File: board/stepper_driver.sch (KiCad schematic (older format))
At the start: 28 parts, among them J2301 CONN_STEPPER, P2301 CONN_2, U2301 L6470

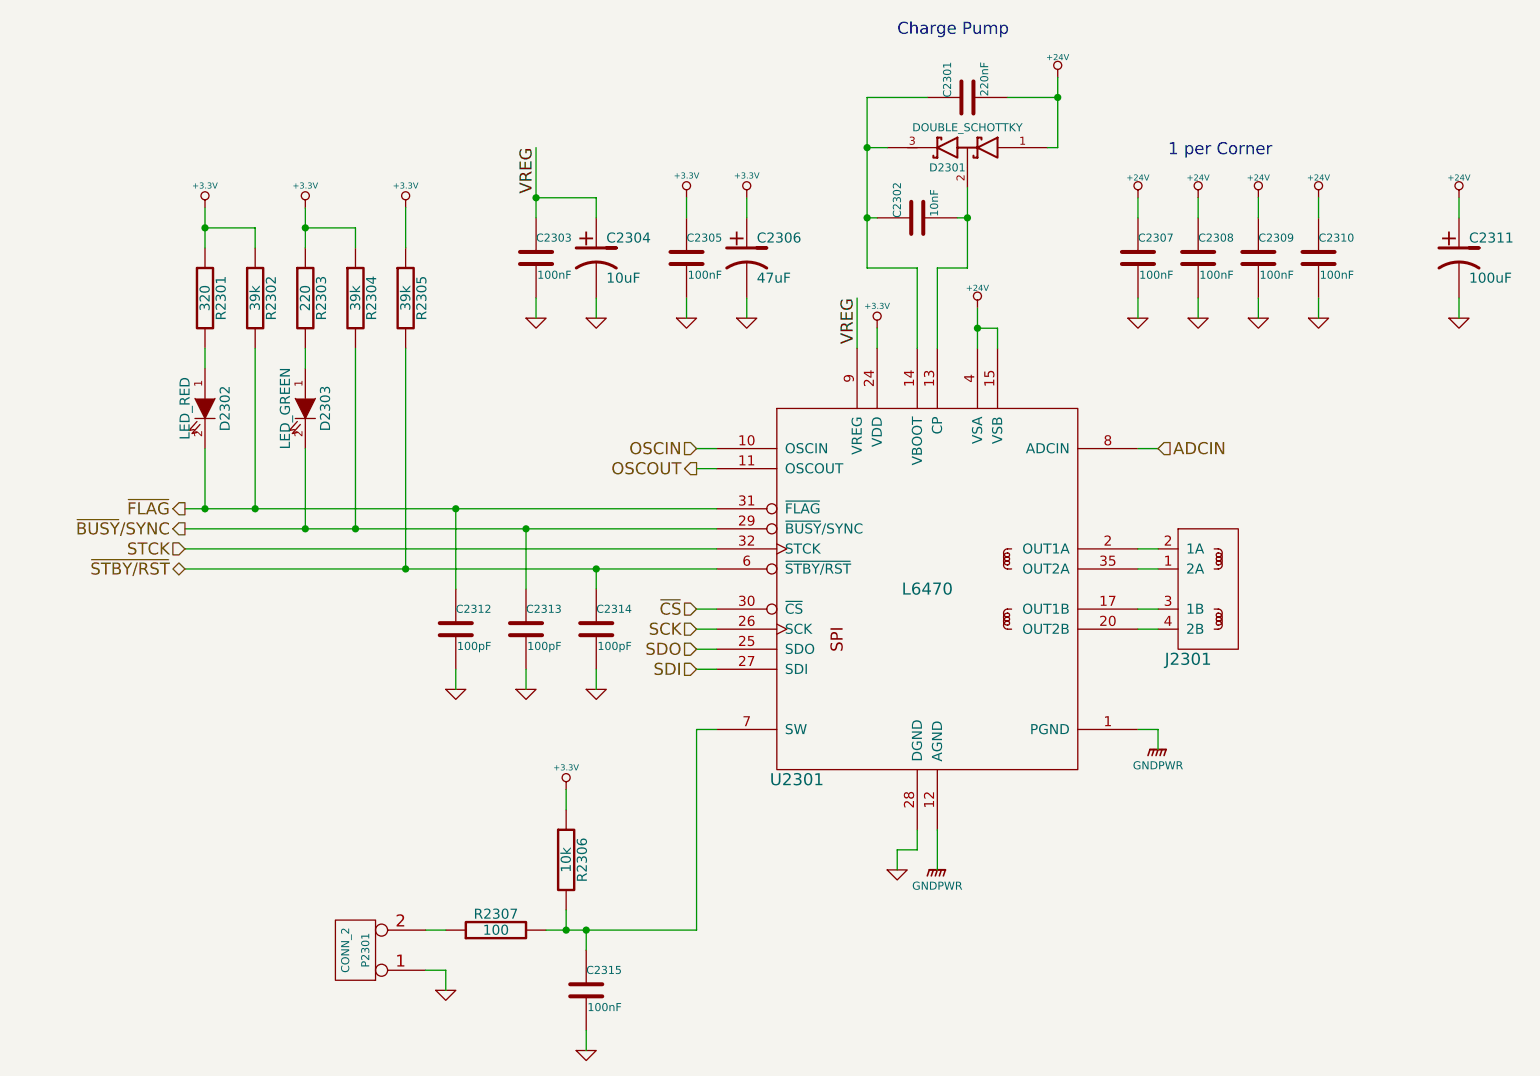
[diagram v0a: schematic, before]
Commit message: Selected Part Numbers for all Components
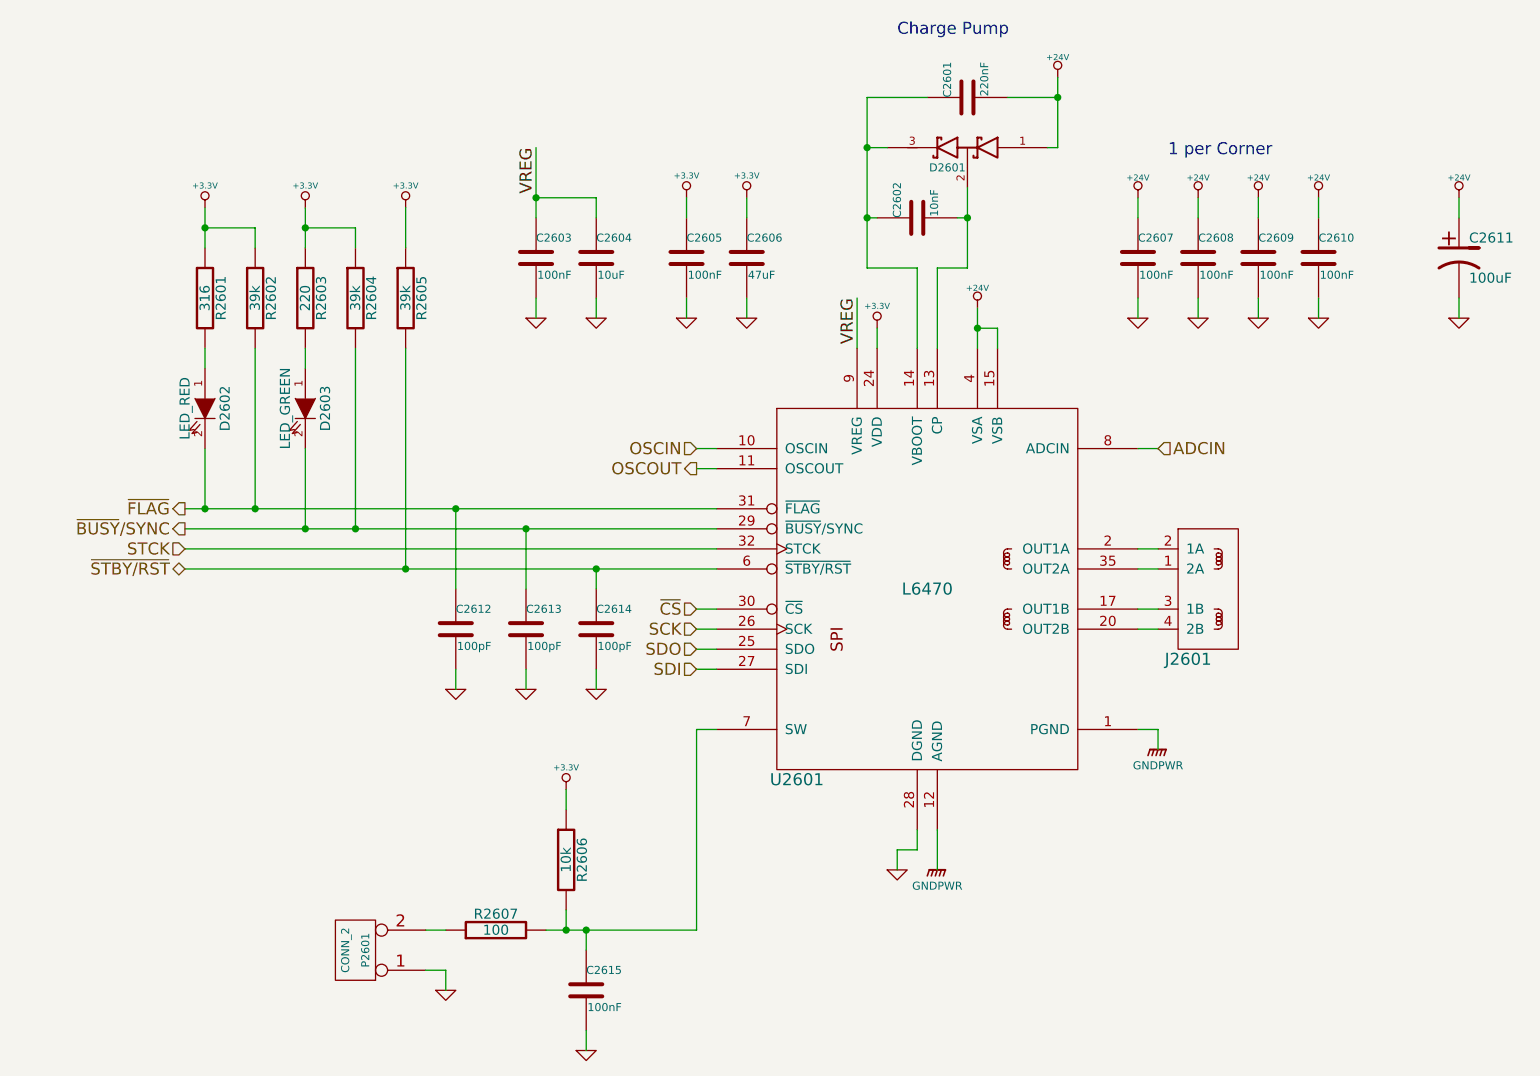
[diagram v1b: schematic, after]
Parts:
- removed C2304: 10uF, symbol CP1
- removed C2306: 47uF, symbol CP1
- added C2304: 10uF, symbol C
- added C2306: 47uF, symbol C
- C2301: Part Number (none) -> CL21B224KCFSFNE
- C2302: Part Number (none) -> C1608X7R2A103K080AA
- C2303, C2305, C2315: Part Number (none) -> CL10F104ZA8NNNC
- C2307, C2308, C2309, C2310: Part Number (none) -> CGA3E3X7S2A104K080AB
- C2311: Part Number (none) -> EEU-EE2C101
- C2312, C2313, C2314: Part Number (none) -> CL10C101JB8NCNC
- J2301: Part Number (none) -> 9993920000
- P2301: Part Number (none) -> 1716020000
- R2301: value 320 -> 316; Part Number (none) -> RC1608F3160CS
- R2302, R2304, R2305: Part Number (none) -> RC1608J393CS
- R2303: Part Number (none) -> RC1608J221CS
- R2306: Part Number (none) -> RC1608J103CS
- R2307: Part Number (none) -> RC1608J101CS
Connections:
- net +3.3V: now also C2306.1
- net GND: now also C2304.2, C2306.2
- net VREG: now also C2304.1

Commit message: Digikey Number + Link
Added a digikey part number and link to all components.
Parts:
- C2301: Digikey Number (none) -> 1276-2949-1-ND; Part Number CL21B224KCFSFNE -> (none)
- C2302: Digikey Number (none) -> 445-1304-1-ND; Part Number C1608X7R2A103K080AA -> (none)
- C2303, C2305, C2315: Digikey Number (none) -> 1276-1011-1-ND; Part Number CL10F104ZA8NNNC -> (none)
- C2304: Digikey Number (none) -> 1276-1119-1-ND; Part Number CL10A106MQ8NNNC -> (none)
- C2306: Digikey Number (none) -> 1276-2420-1-ND; Part Number CL21A476MQCLRNC -> (none)
- C2307, C2308, C2309, C2310: Digikey Number (none) -> 445-6938-1-ND; Part Number CGA3E3X7S2A104K080AB -> (none)
- C2311: Digikey Number (none) -> P13622-ND; Part Number EEU-EE2C101 -> (none)
- C2312, C2313, C2314: Digikey Number (none) -> 1276-2163-1-ND; Part Number CL10C101JB8NCNC -> (none)
- D2301: Digikey Number (none) -> BAS70-04TPMSCT-ND; Part Number BAS70-04-TP -> (none)
- D2302: Digikey Number (none) -> 67-1551-1-ND; Part Number SML-LX0603SRW-TR -> (none)
- D2303: Digikey Number (none) -> 67-1693-1-ND; Part Number SML-LX0603SUGW-TR -> (none)
- J2301: Digikey Number (none) -> 281-1437-ND; Part Number 9993920000 -> (none)
- P2301: Digikey Number (none) -> 281-1435-ND; Part Number 1716020000 -> (none)
- R2301: Digikey Number (none) -> 1276-4602-1-ND; Part Number RC1608F3160CS -> (none)
- R2302, R2304, R2305: Digikey Number (none) -> 1276-5100-1-ND; Part Number RC1608J393CS -> (none)
- R2303: Digikey Number (none) -> 1276-5046-1-ND; Part Number RC1608J221CS -> (none)
- R2306: Digikey Number (none) -> 1276-5086-1-ND; Part Number RC1608J103CS -> (none)
- R2307: Digikey Number (none) -> 1276-5038-1-ND; Part Number RC1608J101CS -> (none)

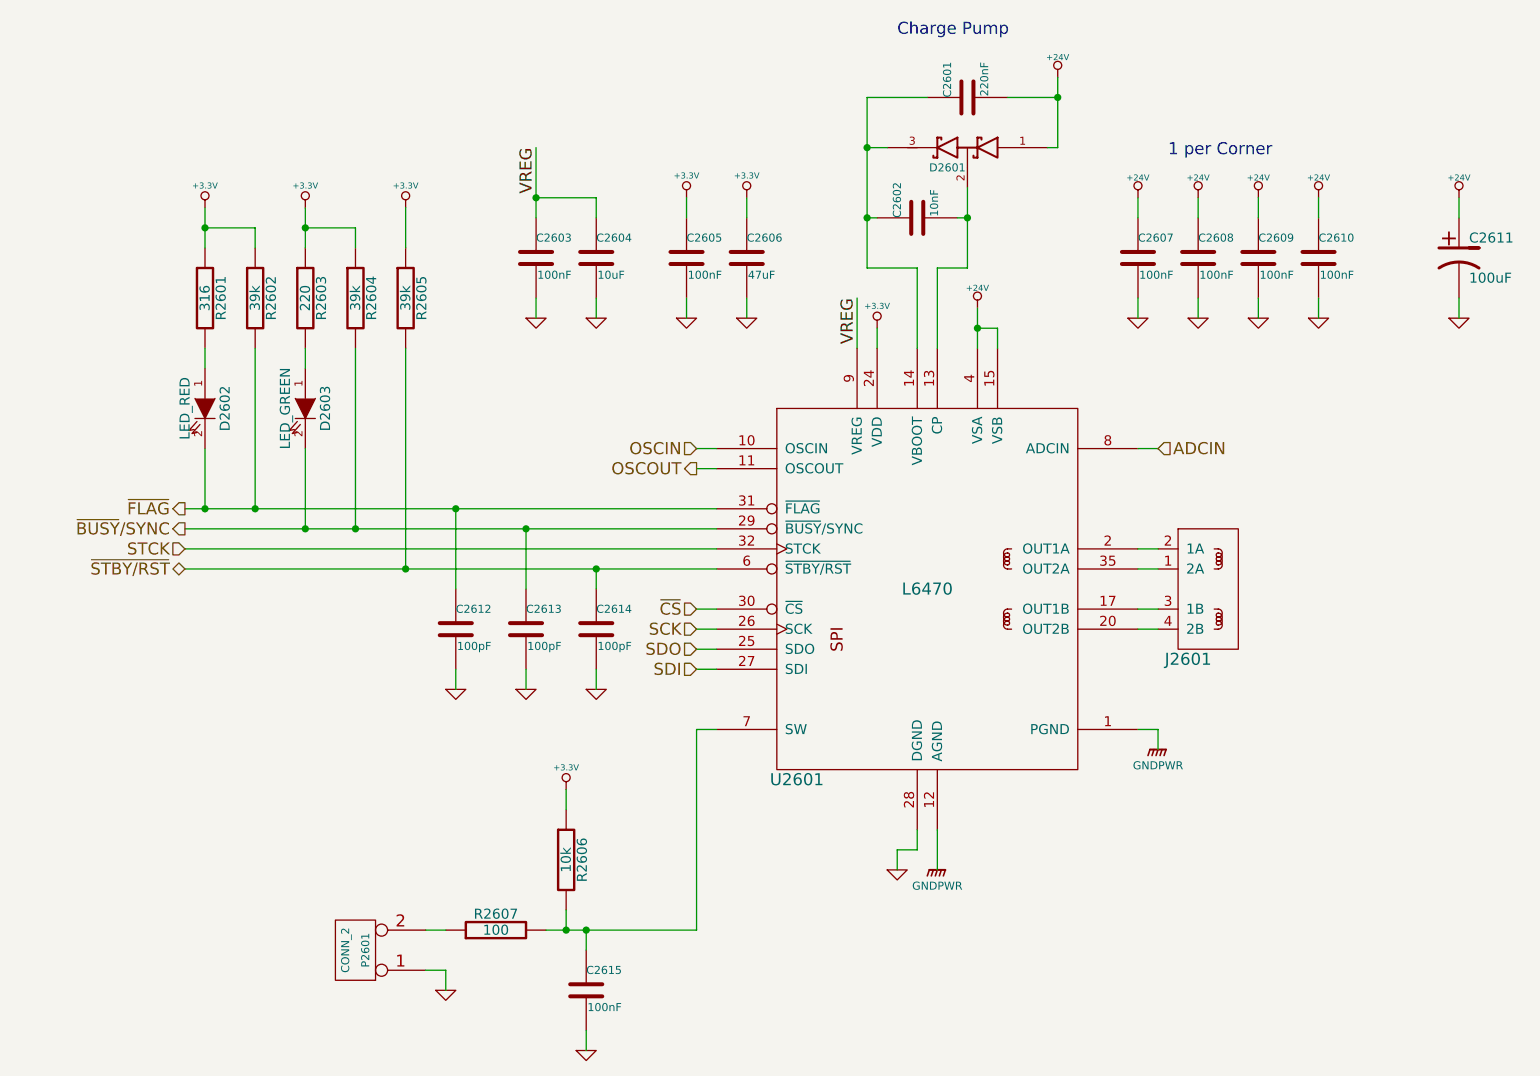
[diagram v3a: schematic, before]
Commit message: Prepared components/footprints for PCB Layout.
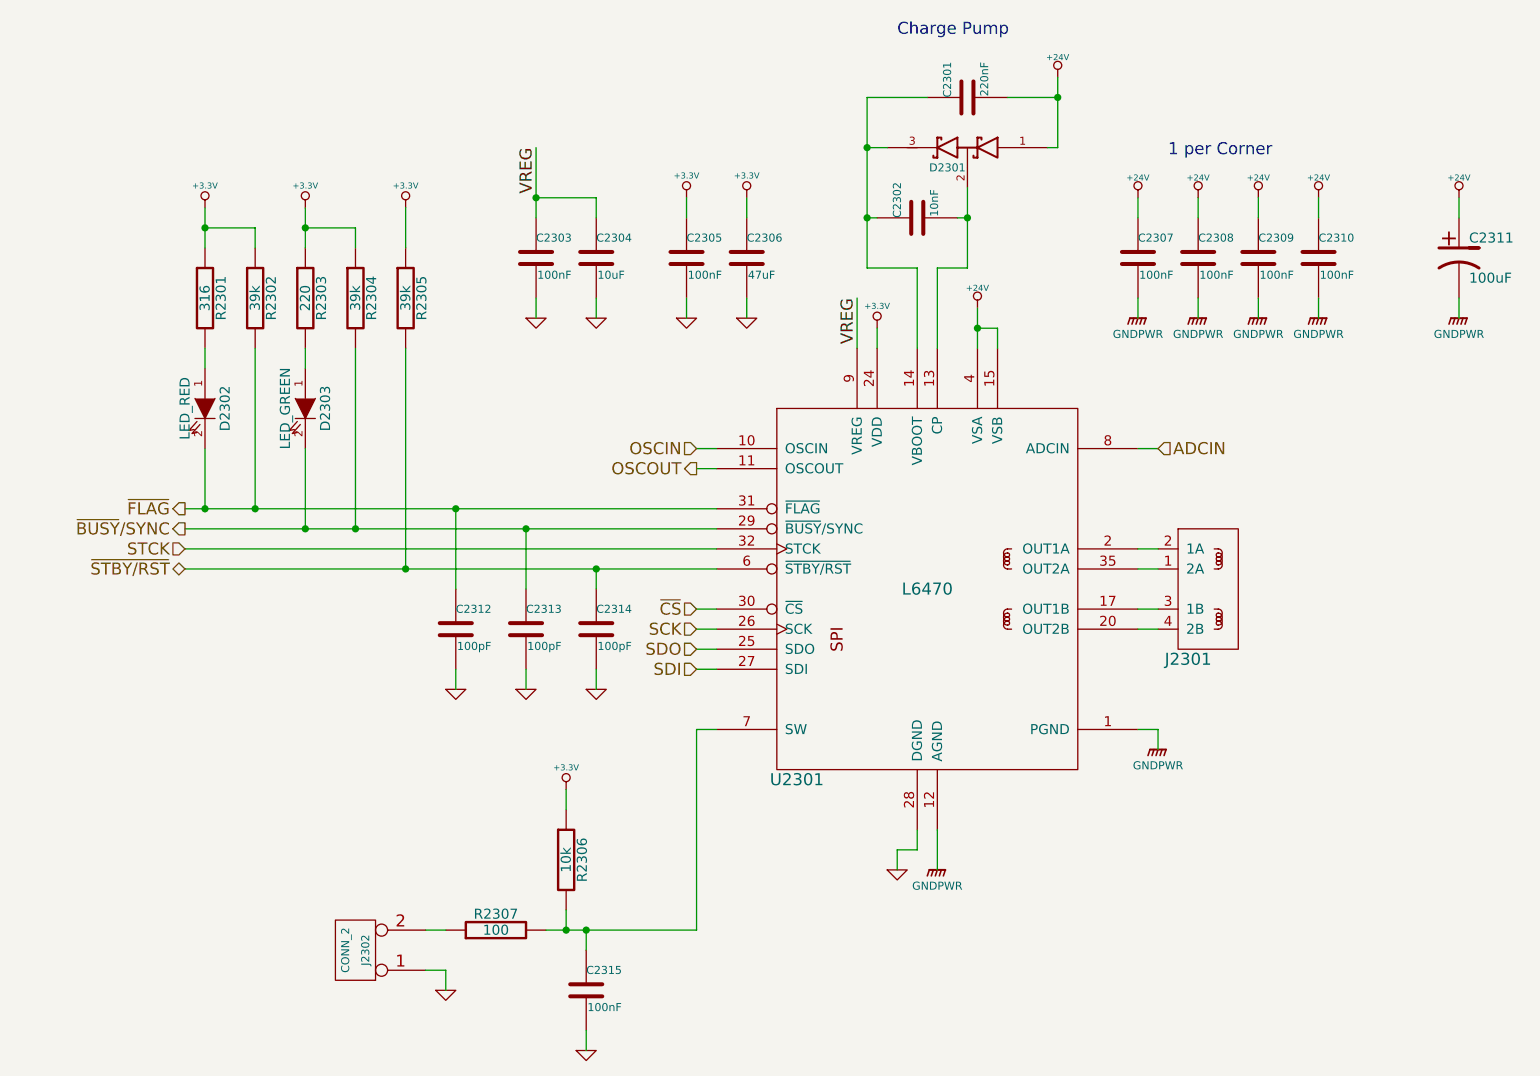
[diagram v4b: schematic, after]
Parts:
- J2301: Digikey Number 281-1437-ND -> (none)
- U2301: Part Number L6470 -> (none)
- renumbered P2301 to J2302
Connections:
- net GND: no longer C2307.2, C2308.2, C2309.2, C2310.2, C2311.2
- net GNDPWR: now also C2307.2, C2308.2, C2309.2, C2310.2, C2311.2

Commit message: Fixed an issue with the CONN_STEPPER
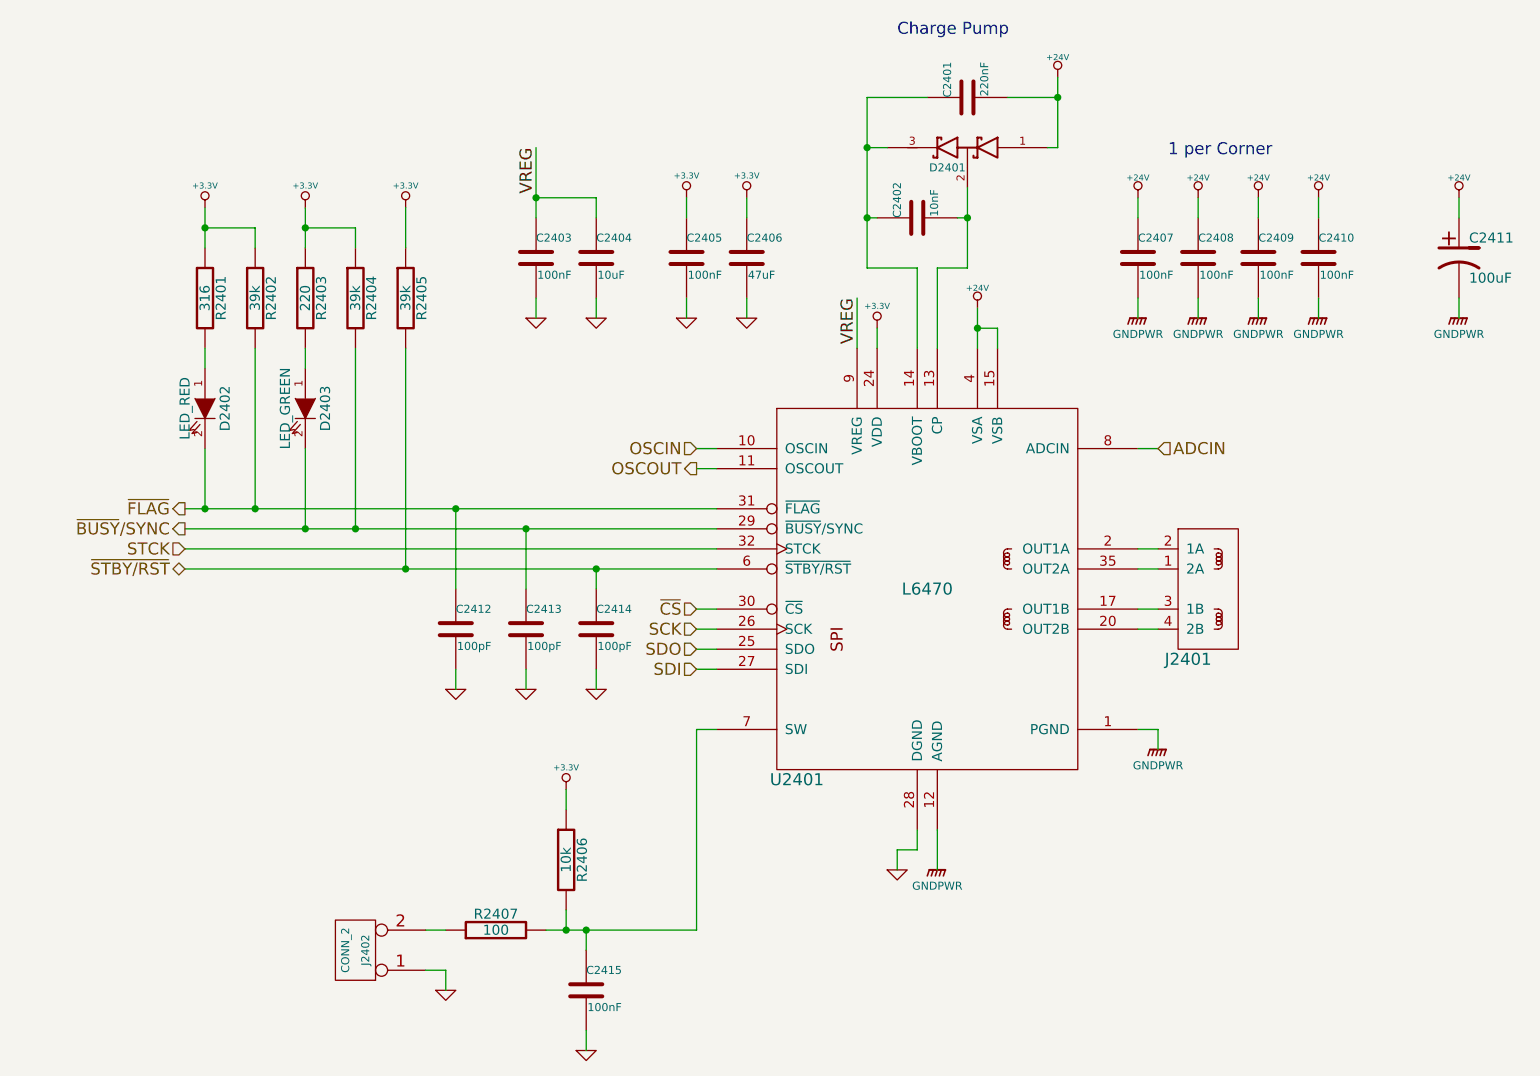
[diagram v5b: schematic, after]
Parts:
- J2301: Digikey Number (none) -> 281-1437-ND
